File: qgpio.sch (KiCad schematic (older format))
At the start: 25 parts, among them J1 I2C_STANDARDQWIIC, J2 I2C_STANDARDQWIIC, J3 Conn_02x10_Odd_Even, U1 PCF8574A

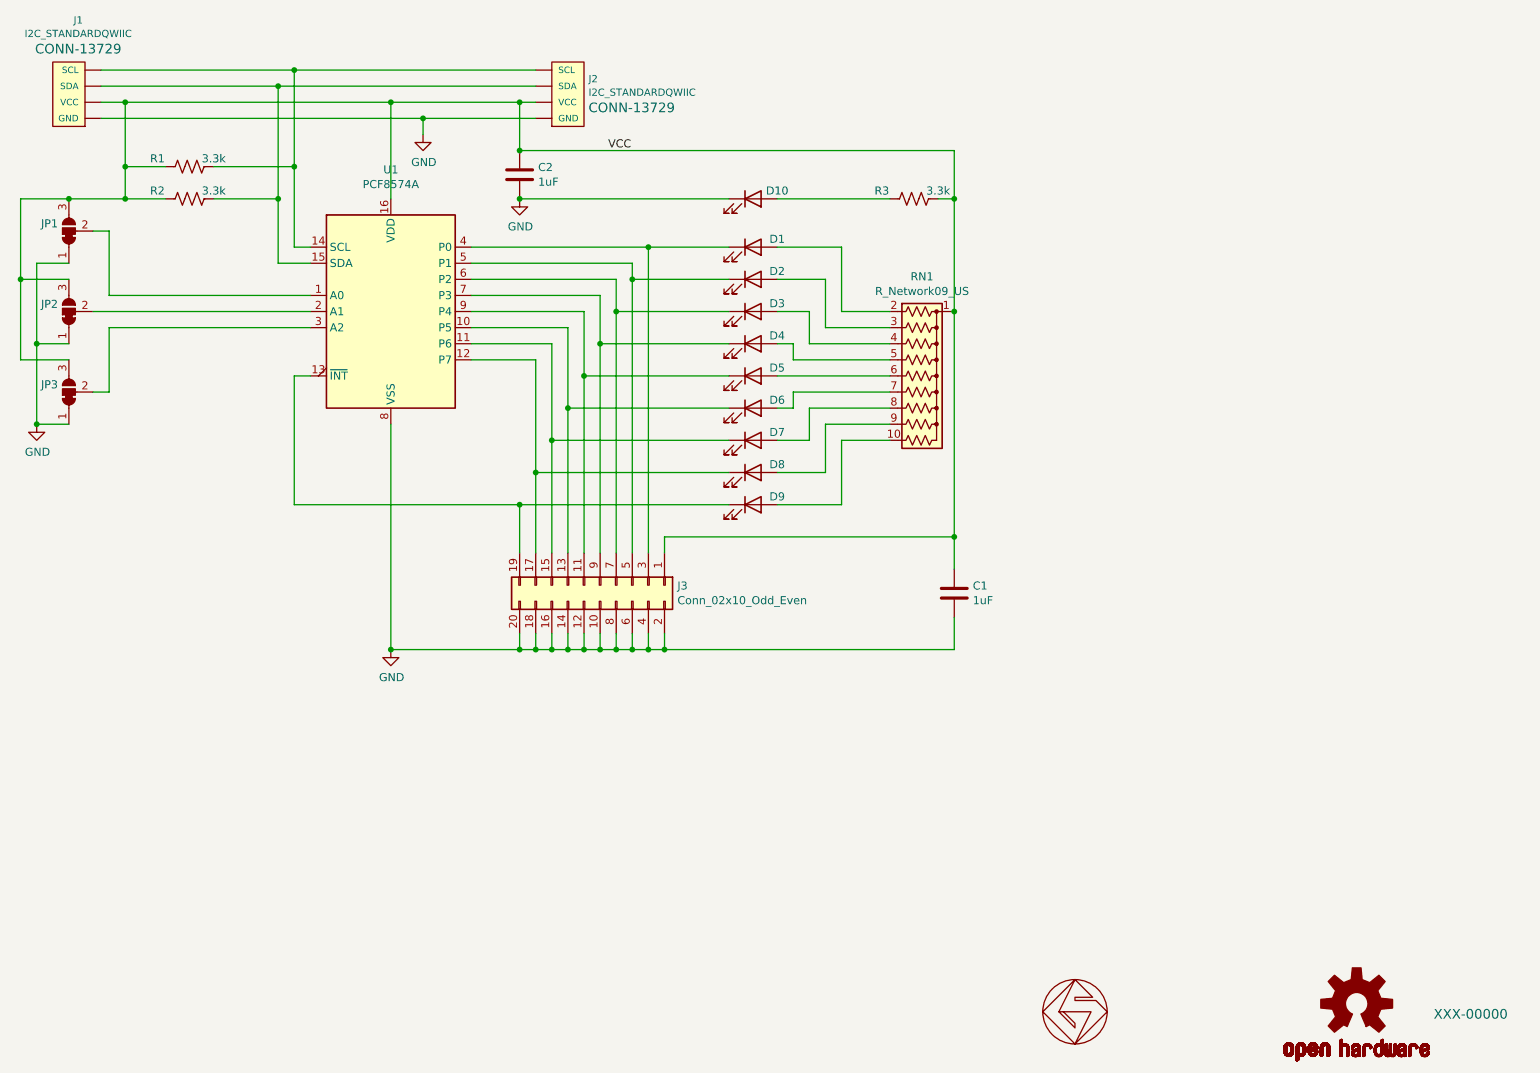
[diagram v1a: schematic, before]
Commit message: cleaned up BOM
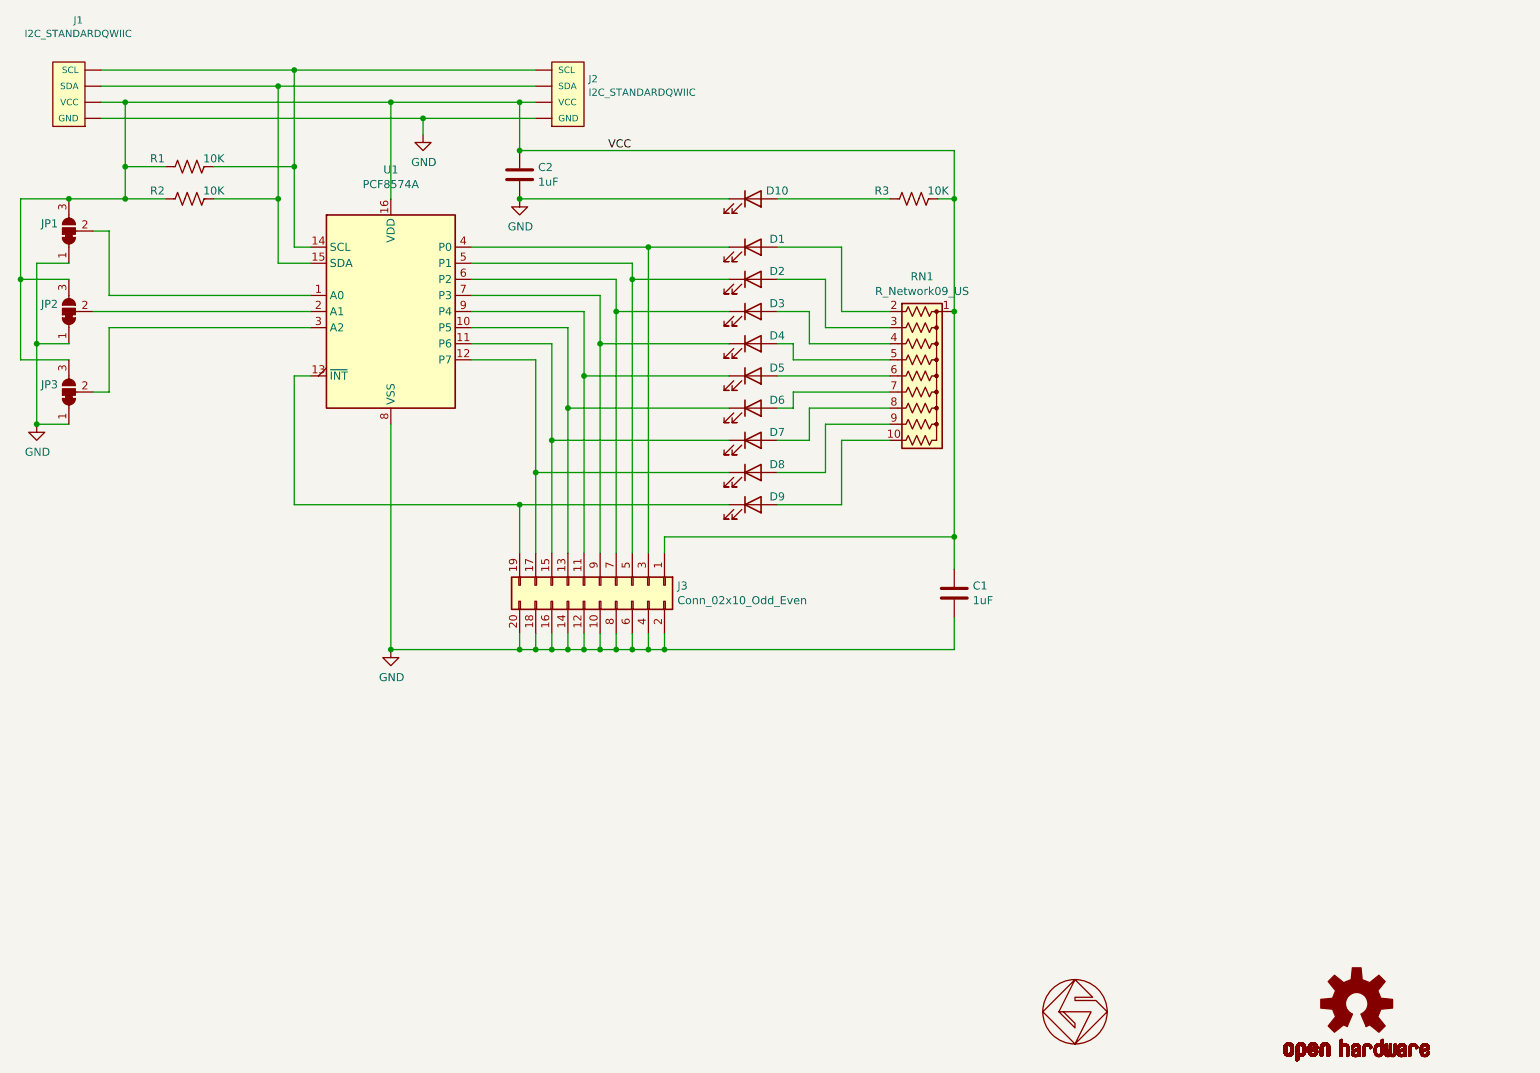
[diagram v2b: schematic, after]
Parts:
- C1, C2: Digikey (none) -> 587-1251-1-ND; MPN (none) -> EMK107BJ105KA-T; Mouser (none) -> 963-EMK107BJ105KA-T
- D1, D10, D2, D3, D4, D5, D6, D7, D8, D9: Digikey (none) -> 160-1435-1-ND; MPN (none) -> LTST-C190KGKT; Mouser (none) -> 859-LTST-C190KGKT
- J1, J2: Digikey (none) -> PRT-14417-ND; Field4 CONN-13729 -> (none); MPN (none) -> PRT-14417; Mouser (none) -> 474-PRT-14417
- J3: Digikey (none) -> 77313-418-20LF-ND; MPN (none) -> 77313-418-20LF; Mouser (none) -> 649-77313-418-20LF
- LOGO1: Field4 XXX-00000 -> (none)
- R1, R2, R3: value 3.3k -> 10K; Digikey (none) -> 311-10KGRCT-ND; MPN (none) -> RC0603JR-0710KL; Mouser (none) -> 603-RC0603JR-0710KL
- RN1: Digikey (none) -> CSC10KCC-ND; MPN (none) -> CSC10A0110K0GEK; Mouser (none) -> 71-CSC10A0110K0GEK
- U1: Digikey (none) -> 568-1074-1-ND; MPN (none) -> PCF8574ATD-T; Mouser (none) -> 771-PCF8574ATD-T
